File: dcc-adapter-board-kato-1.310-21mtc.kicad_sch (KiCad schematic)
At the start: 24 parts

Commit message: 改修
• 21MTC のピン配置がまちがっていた
• アライブキャパシター用端子をなくした
  • +12V・GND パッドを使うようにする
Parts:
- removed C_{Alive}1: C, Connector_Wire:SolderWire-0.1sqmm_1x02_P3.6mm_D0.4mm_OD1mm, symbol Device:C
- removed MOS1: NMOS, Package_TO_SOT_SMD:SOT-563, symbol Device:Q_Dual_NMOS_S1G1D2S2G2D1
- added Q1: NMOSFET1, Package_TO_SOT_SMD:SOT-23, symbol Transistor_FET:DMN2075U
- added Q2: NMOSFET2, Package_TO_SOT_SMD:SOT-23, symbol Transistor_FET:DMN2075U
- renumbered +3.3V1 to VCC1
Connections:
- net GND: now also Q1.2 (S), Q2.2 (S)
- net at 21MTC1.13 (Aux_3): now also Q1.1 (G)
- net at 21MTC1.4 (Aux_4): now also Q2.1 (G)
- net at R_{Rear_Right}1.1: now also Q2.3 (D)
- net at R_{Front_Left}1.1: now also Q1.3 (D)
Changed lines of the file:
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@@
-    )
-  )
-  (global_label "GND" (shape input) (at 233.68 29.21 270) (fields_autoplaced)
-    (effects (font (size 1.27 1.27)) (justify right))
-    (property "Intersheetrefs" "${INTERSHEET_REFS}" (at 233.68 35.9863 90)
-      (effects (font (size 1.27 1.27)) (justify right) hide)
     )
   )
@@
     (effects (font (size 1.27 1.27)) (justify left))
     (property "Intersheetrefs" "${INTERSHEET_REFS}" (at 176.2608 106.68 0)
-      (effects (font (size 1.27 1.27)) (justify left) hide)
-    )
-  )
-  (global_label "+12V" (shape input) (at 233.68 21.59 90) (fields_autoplaced)
-    (effects (font (size 1.27 1.27)) (justify left))
-    (property "Intersheetrefs" "${INTERSHEET_REFS}" (at 233.68 13.6042 90)
       (effects (font (size 1.27 1.27)) (justify left) hide)
     )
@@
     )
   )
-  (symbol (lib_id "Device:C") (at 233.68 25.4 180) (unit 1)
-    (in_bom yes) (on_board yes) (dnp no) (fields_autoplaced)
-    (property "Reference" "C_{Alive}1" (at 236.601 24.7563 0)
-      (effects (font (size 1.27 1.27)) (justify right))
-    )
-    (property "Value" "C" (at 236.601 26.6773 0)
-      (effects (font (size 1.27 1.27)) (justify right))
-    )
-    (property "Footprint" "Connector_Wire:SolderWire-0.1sqmm_1x02_P3.6mm_D0.4mm_OD1mm" (at 232.7148 21.59 0)
-      (effects (font (size 1.27 1.27)) hide)
-    )
-    (property "Datasheet" "~" (at 233.68 25.4 0)
-      (effects (font (size 1.27 1.27)) hide)
-    )
-    (pin "1")
-    (pin "2")
-    (instances
-      (project "dcc-adapter-board-kato-1.310-21mtc"
-        (path "/c9e0287e-0b07-4219-92d3-bfc6081ec238"
-          (reference "C_{Alive}1") (unit 1)
-        )
-      )
-    )
-  )
   (symbol (lib_id "Connector_Generic:Conn_01x01") (at 173.99 52.705 0) (unit 1)
     (in_bom yes) (on_board yes) (dnp no) (fields_autoplaced)
-    (property "Reference" "+3.3V1" (at 176.022 52.0613 0)
+    (property "Reference" "VCC1" (at 176.022 52.0613 0)
       (effects (font (size 1.27 1.27)) (justify left))
     )
@@
       (project "dcc-adapter-board-kato-1.310-21mtc"
         (path "/c9e0287e-0b07-4219-92d3-bfc6081ec238"
-          (reference "+3.3V1") (unit 1)
+          (reference "VCC1") (unit 1)
         )
       )
@@
     )
   )
+  (symbol (lib_id "Transistor_FET:DMN2075U") (at 114.3 102.87 0) (unit 1)
+    (in_bom yes) (on_board yes) (dnp no) (fields_autoplaced)
+    (property "Reference" "Q1" (at 119.507 102.2263 0)
+      (effects (font (size 1.27 1.27)) (justify left))
+    )
+    (property "Value" "NMOSFET1" (at 119.507 104.1473 0)
+      (effects (font (size 1.27 1.27)) (justify left))
+    )
+    (property "Footprint" "Package_TO_SOT_SMD:SOT-23" (at 119.38 104.775 0)
+      (effects (font (size 1.27 1.27) italic) (justify left) hide)
+    )
+    (property "Datasheet" "http://www.diodes.com/assets/Datasheets/DMN2075U.pdf" (at 114.3 102.87 0)
+      (effects (font (size 1.27 1.27)) (justify left) hide)
+    )
+    (pin "1")
+    (pin "2")
+    (pin "3")
+    (instances
+      (project "dcc-adapter-board-kato-1.310-21mtc"
+        (path "/c9e0287e-0b07-4219-92d3-bfc6081ec238"
+          (reference "Q1") (unit 1)
+        )
+      )
+    )
+  )
   (symbol (lib_id "Device:LED") (at 161.29 97.79 0) (unit 1)
     (in_bom yes) (on_board yes) (dnp no) (fields_autoplaced)
@@
     )
   )
-  (symbol (lib_id "Device:Q_Dual_NMOS_S1G1D2S2G2D1") (at 114.3 102.87 0) (unit 1)
-    (in_bom yes) (on_board yes) (dnp no) (fields_autoplaced)
-    (property "Reference" "MOS1" (at 119.507 102.2263 0)
-      (effects (font (size 1.27 1.27)) (justify left))
-    )
-    (property "Value" "NMOS" (at 119.507 104.1473 0)
-      (effects (font (size 1.27 1.27)) (justify left))
-    )
-    (property "Footprint" "Package_TO_SOT_SMD:SOT-563" (at 119.38 102.87 0)
-      (effects (font (size 1.27 1.27)) hide)
-    )
-    (property "Datasheet" "~" (at 119.38 102.87 0)
-      (effects (font (size 1.27 1.27)) hide)
-    )
-    (pin "1")
-    (pin "2")
-    (pin "6")
+  (symbol (lib_id "Connector_Generic:Conn_01x01") (at 173.99 22.225 0) (unit 1)
+    (in_bom yes) (on_board yes) (dnp no) (fields_autoplaced)
+    (property "Reference" "Rail_{Left}1" (at 176.022 21.5813 0)
+      (effects (font (size 1.27 1.27)) (justify left))
+    )
+    (property "Value" "J" (at 176.022 23.5023 0)
+      (effects (font (size 1.27 1.27)) (justify left))
+    )
+    (property "Footprint" "Connector_Wire:SolderWire-1.5sqmm_1x01_D1.7mm_OD3.9mm" (at 173.99 22.225 0)
+      (effects (font (size 1.27 1.27)) hide)
+    )
+    (property "Datasheet" "~" (at 173.99 22.225 0)
+      (effects (font (size 1.27 1.27)) hide)
+    )
+    (pin "1")
+    (instances
+      (project "dcc-adapter-board-kato-1.310-21mtc"
+        (path "/c9e0287e-0b07-4219-92d3-bfc6081ec238"
+          (reference "Rail_{Left}1") (unit 1)
+        )
+      )
+    )
+  )
+  (symbol (lib_id "Device:R") (at 140.97 80.01 90) (unit 1)
+    (in_bom yes) (on_board yes) (dnp no) (fields_autoplaced)
+    (property "Reference" "R_{Rear}1" (at 140.97 75.9841 90)
+      (effects (font (size 1.27 1.27)))
+    )
+    (property "Value" "R" (at 140.97 77.9051 90)
+      (effects (font (size 1.27 1.27)))
+    )
+    (property "Footprint" "Resistor_SMD:R_0603_1608Metric_Pad0.98x0.95mm_HandSolder" (at 140.97 81.788 90)
+      (effects (font (size 1.27 1.27)) hide)
+    )
+    (property "Datasheet" "~" (at 140.97 80.01 0)
+      (effects (font (size 1.27 1.27)) hide)
+    )
+    (pin "1")
+    (pin "2")
+    (instances
+      (project "dcc-adapter-board-kato-1.310-21mtc"
+        (path "/c9e0287e-0b07-4219-92d3-bfc6081ec238"
+          (reference "R_{Rear}1") (unit 1)
+        )
+      )
+    )
+  )
+  (symbol (lib_id "Transistor_FET:DMN2075U") (at 127.635 111.76 0) (unit 1)
+    (in_bom yes) (on_board yes) (dnp no)
+    (property "Reference" "Q2" (at 118.11 118.11 0)
+      (effects (font (size 1.27 1.27)) (justify left))
+    )
+    (property "Value" "NMOSFET2" (at 118.11 120.031 0)
+      (effects (font (size 1.27 1.27)) (justify left))
+    )
+    (property "Footprint" "Package_TO_SOT_SMD:SOT-23" (at 132.715 113.665 0)
+      (effects (font (size 1.27 1.27) italic) (justify left) hide)
+    )
+    (property "Datasheet" "http://www.diodes.com/assets/Datasheets/DMN2075U.pdf" (at 127.635 111.76 0)
+      (effects (font (size 1.27 1.27)) (justify left) hide)
+    )
+    (pin "1")
+    (pin "2")
     (pin "3")
-    (pin "4")
-    (pin "5")
-    (instances
-      (project "dcc-adapter-board-kato-1.310-21mtc"
-        (path "/c9e0287e-0b07-4219-92d3-bfc6081ec238"
-          (reference "MOS1") (unit 1)
-        )
-      )
-    )
-  )
-  (symbol (lib_id "Connector_Generic:Conn_01x01") (at 173.99 22.225 0) (unit 1)
-    (in_bom yes) (on_board yes) (dnp no) (fields_autoplaced)
-    (property "Reference" "Rail_{Left}1" (at 176.022 21.5813 0)
-      (effects (font (size 1.27 1.27)) (justify left))
-    )
-    (property "Value" "J" (at 176.022 23.5023 0)
-      (effects (font (size 1.27 1.27)) (justify left))
-    )
-    (property "Footprint" "Connector_Wire:SolderWire-1.5sqmm_1x01_D1.7mm_OD3.9mm" (at 173.99 22.225 0)
-      (effects (font (size 1.27 1.27)) hide)
-    )
-    (property "Datasheet" "~" (at 173.99 22.225 0)
-      (effects (font (size 1.27 1.27)) hide)
-    )
-    (pin "1")
-    (instances
-      (project "dcc-adapter-board-kato-1.310-21mtc"
-        (path "/c9e0287e-0b07-4219-92d3-bfc6081ec238"
-          (reference "Rail_{Left}1") (unit 1)
-        )
-      )
-    )
-  )
-  (symbol (lib_id "Device:Q_Dual_NMOS_S1G1D2S2G2D1") (at 127.635 111.76 0) (unit 2)
-    (in_bom yes) (on_board yes) (dnp no) (fields_autoplaced)
-    (property "Reference" "MOS1" (at 132.842 111.1163 0)
-      (effects (font (size 1.27 1.27)) (justify left))
-    )
-    (property "Value" "NMOS" (at 132.842 113.0373 0)
-      (effects (font (size 1.27 1.27)) (justify left))
-    )
-    (property "Footprint" "Package_TO_SOT_SMD:SOT-563" (at 132.715 111.76 0)
-      (effects (font (size 1.27 1.27)) hide)
-    )
-    (property "Datasheet" "~" (at 132.715 111.76 0)
-      (effects (font (size 1.27 1.27)) hide)
-    )
-    (pin "1")
-    (pin "2")
-    (pin "6")
-    (pin "3")
-    (pin "4")
-    (pin "5")
-    (instances
-      (project "dcc-adapter-board-kato-1.310-21mtc"
-        (path "/c9e0287e-0b07-4219-92d3-bfc6081ec238"
-          (reference "MOS1") (unit 2)
-        )
-      )
-    )
-  )
-  (symbol (lib_id "Device:R") (at 140.97 80.01 90) (unit 1)
-    (in_bom yes) (on_board yes) (dnp no) (fields_autoplaced)
-    (property "Reference" "R_{Rear}1" (at 140.97 75.9841 90)
-      (effects (font (size 1.27 1.27)))
-    )
-    (property "Value" "R" (at 140.97 77.9051 90)
-      (effects (font (size 1.27 1.27)))
-    )
-    (property "Footprint" "Resistor_SMD:R_0603_1608Metric_Pad0.98x0.95mm_HandSolder" (at 140.97 81.788 90)
-      (effects (font (size 1.27 1.27)) hide)
-    )
-    (property "Datasheet" "~" (at 140.97 80.01 0)
-      (effects (font (size 1.27 1.27)) hide)
-    )
-    (pin "1")
-    (pin "2")
-    (instances
-      (project "dcc-adapter-board-kato-1.310-21mtc"
-        (path "/c9e0287e-0b07-4219-92d3-bfc6081ec238"
-          (reference "R_{Rear}1") (unit 1)
-        )
-      )
+    (instances
+      (project "dcc-adapter-board-kato-1.310-21mtc"
+        (path "/c9e0287e-0b07-4219-92d3-bfc6081ec238"
+          (reference "Q2") (unit 1)
+        )
+      )

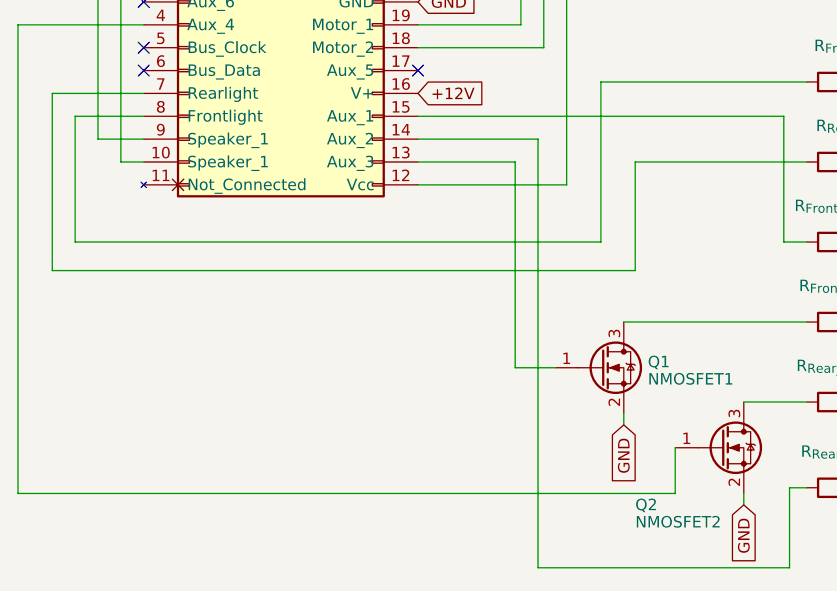
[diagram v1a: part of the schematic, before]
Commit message: v2 フィードバック
• MOSFET のゲートの前段に抵抗を追加
• ねじ穴の位置を 0.5mm 外側に移動
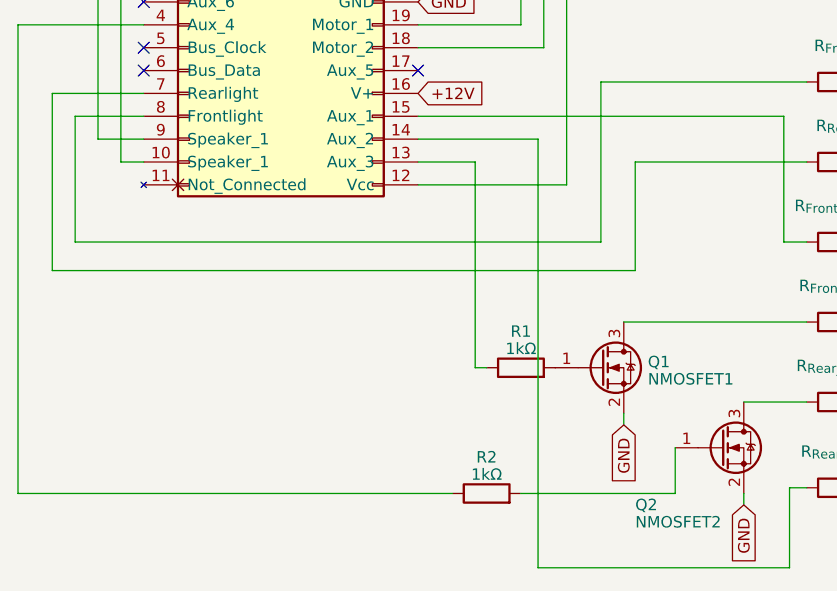
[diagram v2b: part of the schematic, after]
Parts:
- added R1, R2: 1kΩ, Resistor_SMD:R_0603_1608Metric_Pad0.98x0.95mm_HandSolder, symbol Device:R
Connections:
- net at 21MTC1.13 (Aux_3): now also R1.1; no longer Q1.1 (G)
- net at 21MTC1.4 (Aux_4): now also R2.1; no longer Q2.1 (G)
- new net: Q2.1 (G), R2.2
- new net: Q1.1 (G), R1.2
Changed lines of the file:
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@@
-    (stroke (width 0) (type default))
-  )
-  (wire (pts (xy 104.775 102.87) (xy 104.775 80.01))
     (stroke (width 0) (type default))
   )
@@
     (stroke (width 0) (type default))
   )
-  (wire (pts (xy 104.775 80.01) (xy 93.98 80.01))
-    (stroke (width 0) (type default))
-  )
   (wire (pts (xy 53.34 72.39) (xy 63.5 72.39))
     (stroke (width 0) (type default))
@@
     (stroke (width 0) (type default))
   )
-  (wire (pts (xy 122.555 116.84) (xy 49.53 116.84))
+  (wire (pts (xy 122.555 116.84) (xy 105.41 116.84))
     (stroke (width 0) (type default))
   )
@@
     (stroke (width 0) (type default))
   )
+  (wire (pts (xy 100.33 80.01) (xy 100.33 102.87))
+    (stroke (width 0) (type default))
+  )
   (wire (pts (xy 168.91 27.305) (xy 105.41 27.305))
     (stroke (width 0) (type default))
@@
     (stroke (width 0) (type default))
   )
+  (wire (pts (xy 97.79 116.84) (xy 49.53 116.84))
+    (stroke (width 0) (type default))
+  )
   (wire (pts (xy 116.84 97.79) (xy 137.16 97.79))
     (stroke (width 0) (type default))
@@
     (stroke (width 0) (type default))
   )
+  (wire (pts (xy 93.98 80.01) (xy 100.33 80.01))
+    (stroke (width 0) (type default))
+  )
   (wire (pts (xy 102.87 22.225) (xy 168.91 22.225))
     (stroke (width 0) (type default))
@@
     (stroke (width 0) (type default))
   )
-  (wire (pts (xy 104.775 102.87) (xy 109.22 102.87))
-    (stroke (width 0) (type default))
-  )
   (wire (pts (xy 55.88 88.9) (xy 55.88 74.93))
+    (stroke (width 0) (type default))
+  )
+  (wire (pts (xy 100.33 102.87) (xy 101.6 102.87))
     (stroke (width 0) (type default))
   )
@@
     )
   )
+  (symbol (lib_id "Device:R") (at 101.6 116.84 90) (unit 1)
+    (in_bom yes) (on_board yes) (dnp no) (fields_autoplaced)
+    (property "Reference" "R2" (at 101.6 112.8141 90)
+      (effects (font (size 1.27 1.27)))
+    )
+    (property "Value" "1kΩ" (at 101.6 114.7351 90)
+      (effects (font (size 1.27 1.27)))
+    )
+    (property "Footprint" "Resistor_SMD:R_0603_1608Metric_Pad0.98x0.95mm_HandSolder" (at 101.6 118.618 90)
+      (effects (font (size 1.27 1.27)) hide)
+    )
+    (property "Datasheet" "~" (at 101.6 116.84 0)
+      (effects (font (size 1.27 1.27)) hide)
+    )
+    (pin "1")
+    (pin "2")
+    (instances
+      (project "dcc-adapter-board-kato-1.310-21mtc"
+        (path "/c9e0287e-0b07-4219-92d3-bfc6081ec238"
+          (reference "R2") (unit 1)
+        )
+      )
+    )
+  )
   (symbol (lib_id "Device:R") (at 140.97 97.79 90) (unit 1)
     (in_bom yes) (on_board yes) (dnp no) (fields_autoplaced)
@@
         )
       )
+    )
+  )
+  (symbol (lib_id "Device:R") (at 105.41 102.87 90) (unit 1)
+    (in_bom yes) (on_board yes) (dnp no) (fields_autoplaced)
+    (property "Reference" "R1" (at 105.41 98.8441 90)
+      (effects (font (size 1.27 1.27)))
+    )
+    (property "Value" "1kΩ" (at 105.41 100.7651 90)
+      (effects (font (size 1.27 1.27)))
+    )
+    (property "Footprint" "Resistor_SMD:R_0603_1608Metric_Pad0.98x0.95mm_HandSolder" (at 105.41 104.648 90)
+      (effects (font (size 1.27 1.27)) hide)
+    )
+    (property "Datasheet" "~" (at 105.41 102.87 0)
+      (effects (font (size 1.27 1.27)) hide)
+    )
+    (pin "1")
+    (pin "2")
+    (instances
+      (project "dcc-adapter-board-kato-1.310-21mtc"
+        (path "/c9e0287e-0b07-4219-92d3-bfc6081ec238"
+          (reference "R1") (unit 1)
+        )
+      )
